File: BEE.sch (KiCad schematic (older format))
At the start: 53 parts, among them J1 RPI1_header, J10 Conn_01x02, J11 Conn_01x02, J12 Conn_01x02, J13 Conn_01x06, J14 Conn_01x03, J16 Conn_01x08, J17 Conn_01x03, J18 Conn_01x03, J2 Conn_02x05_Odd_Even, J3 Conn_02x03_Odd_Even, J4 Conn_01x06, J5 Conn_02x10_Odd_Even, J7 Conn_02x08_Odd_Even, J8 Conn_02x08_Top_Bottom, J9 Conn_01x02, SW1 SW_Push, SW2 SW_Push, SW3 SW_Push, U1 MCP3008, U2 MCP4911

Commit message: first version with display and dip switches
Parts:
- removed J3: Conn_02x03_Odd_Even, Connector_PinHeader_2.54mm:PinHeader_2x03_P2.54mm_Vertical, symbol Connector_Generic:Conn_02x03_Odd_Even
- removed J8: Conn_02x08_Top_Bottom, Connector_PinHeader_2.54mm:PinHeader_2x08_P2.54mm_Vertical, symbol Connector_Generic:Conn_02x08_Odd_Even
- removed U1: MCP3008, Package_SO:SOIC-16_3.9x9.9mm_P1.27mm, symbol Analog_ADC:MCP3008
- added C4: 0.1uF, Capacitor_SMD:C_0805_2012Metric_Pad1.18x1.45mm_HandSolder, symbol Device:C
- added J3: Conn_01x03, Connector_PinHeader_2.54mm:PinHeader_1x03_P2.54mm_Vertical, symbol Connector_Generic:Conn_01x03
- added J6: Conn_01x06, Connector_PinHeader_2.54mm:PinHeader_1x06_P2.54mm_Vertical, symbol Connector_Generic:Conn_01x06
- added R16, R17, R18, R19, R20, R21, R22, R23: 220, Resistor_SMD:R_0805_2012Metric_Pad1.20x1.40mm_HandSolder, symbol Device:R
- added U1: MCP3008, Package_SO:SOIC-16_3.9x9.9mm_P1.27mm, symbol BEE:MCP3008
- added U3, U4: Dip_08xsp3t, BEElib:dip_08xsp3t, symbol BEE:Dip_08xsp3t
- added U5: 74HC595, Package_SO:SOIC-16_3.9x9.9mm_P1.27mm, symbol 74xx:74HC595
- added U6: Display_7Segments, BEElib:7segments, symbol BEE:Display_7Segments
- C1, C2, C3: footprint Capacitor_SMD:C_0805_2012Metric_Pad1.15x1.40mm_HandSolder -> Capacitor_SMD:C_0805_2012Metric_Pad1.18x1.45mm_HandSolder
- R1, R15, R2, R3, R4, R5, R6, R7, R8: footprint Resistor_SMD:R_0805_2012Metric_Pad1.15x1.40mm_HandSolder -> Resistor_SMD:R_0805_2012Metric_Pad1.20x1.40mm_HandSolder
- R10: renamed from R9; footprint Resistor_SMD:R_0805_2012Metric_Pad1.15x1.40mm_HandSolder -> Resistor_SMD:R_0805_2012Metric_Pad1.20x1.40mm_HandSolder
- R11: renamed from R13; footprint Resistor_SMD:R_0805_2012Metric_Pad1.15x1.40mm_HandSolder -> Resistor_SMD:R_0805_2012Metric_Pad1.20x1.40mm_HandSolder
- R12: renamed from R14; footprint Resistor_SMD:R_0805_2012Metric_Pad1.15x1.40mm_HandSolder -> Resistor_SMD:R_0805_2012Metric_Pad1.20x1.40mm_HandSolder
- R13: renamed from R10; footprint Resistor_SMD:R_0805_2012Metric_Pad1.15x1.40mm_HandSolder -> Resistor_SMD:R_0805_2012Metric_Pad1.20x1.40mm_HandSolder
- R14: renamed from R11; footprint Resistor_SMD:R_0805_2012Metric_Pad1.15x1.40mm_HandSolder -> Resistor_SMD:R_0805_2012Metric_Pad1.20x1.40mm_HandSolder
- R9: renamed from R12; footprint Resistor_SMD:R_0805_2012Metric_Pad1.15x1.40mm_HandSolder -> Resistor_SMD:R_0805_2012Metric_Pad1.20x1.40mm_HandSolder
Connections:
- net labels added: BCM18, QH', RCLK, SER, SRCLK, nOE, nSRCLR
- net labels removed: AR0, AR1, AR2, AR3, AR4, AR5, AR6, AR7, BCM18_PWM0
- wire segments 246 -> 275
- no-connect marks 6 -> 5
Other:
- note added: "7/8 Segment Display Driver"
- note added: "QH'"
- note added: "RCLK"
- note added: "SER"
- note added: "SRCLK"
- note added: "Socket (feemale)"
- note added: "UART: FTDI cables:\n1 - Black -> gnd\n2 - Brown -> CTS\n3 - Red -> Vcc\n4 - Orange -> TX\n5 - Yellow -> RX\n6 - Green -> RTS\n\nWe connect them crossed"
- note added: "nOE"
- note added: "nSRCLR\n"
- note removed: "Resistor set to polarrize external analog sensors"
- note removed: "UART. TDI cables:\n1 - Black -> gnd\n2 - Brown -> CTS\n3 - Red -> Vcc\n4 - Orange -> TX\n5 - Yellow -> RX\n6 - Green -> RTS\n\nWe connect them crossed"
- moved on the sheet: BZ1, C1, C2, C3, FID1, FID2, FID3, H1, H2, H3, H4, J10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

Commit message: Bypass cap for Shifter, DAC cap symbol fix, DAC out pin headers reorganization, labels and fab layer cleanup.
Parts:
- added C5: 0.1uF, Capacitor_SMD:C_0805_2012Metric_Pad1.18x1.45mm_HandSolder, symbol Device:C
- C3: footprint Capacitor_SMD:C_0805_2012Metric_Pad1.18x1.45mm_HandSolder -> Capacitor_Tantalum_SMD:CP_EIA-2012-15_AVX-P_Pad1.30x1.05mm_HandSolder; symbol Device:C -> Device:CP1
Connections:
- net GND: now also C5.1
- net at J10.1 (Pin_1), U2.6 (Vref): now also C5.2
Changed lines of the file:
@@
 	9455 3405 9505 3405
 Wire Wire Line
-	8955 3305 9355 3305
+	8955 3305 9025 3305
 $Comp
 L power:PWR_FLAG #FLG0102
@@
 Wire Wire Line
 	8055 3605 8355 3605
-$Comp
-L Device:C C2
-U 1 1 5D974B40
-P 8355 3055
-F 0 "C2" V 8305 3155 50  0000 C CNN
-F 1 "0.1uF" V 8255 2905 50  0000 C CNN
-F 2 "Capacitor_SMD:C_0805_2012Metric_Pad1.18x1.45mm_HandSolder" H 8393 2905 50  0001 C CNN
-F 3 "https://www.mouser.es/datasheet/2/212/KEM_C1002_X7R_SMD-1102033.pdf" H 8355 3055 50  0001 C CNN
-F 4 "Mouser" H 5   -195 50  0001 C CNN "Distributor"
-F 5 "80-C0805C104K3R" H 5   -195 50  0001 C CNN "Distributor PN"
-F 6 "https://www.mouser.es/ProductDetail/KEMET/C0805C104K3RACTU?qs=sGAEpiMZZMs0AnBnWHyRQFCCI5cSbRT%2FqS%252BgegeU2mQ%3D" H 5   -195 50  0001 C CNN "Distributor link"
-F 7 "KEMET" H 5   -195 50  0001 C CNN "Manufacturer"
-F 8 "C0805C104K3RACTU" H 5   -195 50  0001 C CNN "Manufacturer PN"
-	1    8355 3055
-	0    1    1    0
-$EndComp
-$Comp
-L Device:C C3
-U 1 1 5D974BE9
-P 8355 3255
-F 0 "C3" V 8305 3355 50  0000 C CNN
-F 1 "10uF" V 8305 3105 50  0000 C CNN
-F 2 "Capacitor_SMD:C_0805_2012Metric_Pad1.18x1.45mm_HandSolder" H 8393 3105 50  0001 C CNN
-F 3 "https://www.mouser.es/datasheet/2/40/TAJ_LOW_PROFILE-932651.pdf" H 8355 3255 50  0001 C CNN
-F 4 "Mouser" H 5   -195 50  0001 C CNN "Distributor"
-F 5 " 581-TAJP106K006RNJ " H 5   -195 50  0001 C CNN "Distributor PN"
-F 6 "https://www.mouser.es/ProductDetail/AVX/TAJP106K006RNJ?qs=q%252BHV0zBR8MhWDNAZ3JBdYA%3D%3D" H 5   -195 50  0001 C CNN "Distributor link"
-F 7 "AVX" H 5   -195 50  0001 C CNN "Manufacturer"
-F 8 "TAJP106K006RNJ " H 5   -195 50  0001 C CNN "Manufacturer PN"
-	1    8355 3255
-	0    1    1    0
-$EndComp
 Connection ~ 8755 3255
 Wire Wire Line
@@
 Text Label 7915 1945 0    50   ~ 0
 QH'
+$Comp
+L Device:C C5
+U 1 1 62DC27FC
+P 9025 3155
+F 0 "C5" V 8975 3255 50  0000 C CNN
+F 1 "0.1uF" V 8890 3155 50  0000 C CNN
+F 2 "Capacitor_SMD:C_0805_2012Metric_Pad1.18x1.45mm_HandSolder" H 9063 3005 50  0001 C CNN
+F 3 "https://www.mouser.es/datasheet/2/212/KEM_C1002_X7R_SMD-1102033.pdf" H 9025 3155 50  0001 C CNN
+F 4 "Mouser" H 675 -95 50  0001 C CNN "Distributor"
+F 5 "80-C0805C104K3R" H 675 -95 50  0001 C CNN "Distributor PN"
+F 6 "https://www.mouser.es/ProductDetail/KEMET/C0805C104K3RACTU?qs=sGAEpiMZZMs0AnBnWHyRQFCCI5cSbRT%2FqS%252BgegeU2mQ%3D" H 675 -95 50  0001 C CNN "Distributor link"
+F 7 "KEMET" H 675 -95 50  0001 C CNN "Manufacturer"
+F 8 "C0805C104K3RACTU" H 675 -95 50  0001 C CNN "Manufacturer PN"
+	1    9025 3155
+	1    0    0    -1
+$EndComp
+Connection ~ 9025 3305
+Wire Wire Line
+	9025 3305 9355 3305
+$Comp
+L power:GND #PWR038
+U 1 1 62DC48E1
+P 9215 2955
+F 0 "#PWR038" H 9215 2705 50  0001 C CNN
+F 1 "GND" H 9315 2955 50  0000 C CNN
+F 2 "" H 9215 2955 50  0001 C CNN
+F 3 "" H 9215 2955 50  0001 C CNN
+	1    9215 2955
+	1    0    0    -1
+$EndComp
+Wire Wire Line
+	9215 2955 9215 2945
+Wire Wire Line
+	9215 2945 9025 2945
+Wire Wire Line
+	9025 2945 9025 3005
+$Comp
+L Device:CP1 C3
+U 1 1 5D974BE9
+P 8355 3255
+F 0 "C3" V 8485 3255 50  0000 C CNN
+F 1 "10uF" V 8305 3105 50  0000 C CNN
+F 2 "Capacitor_Tantalum_SMD:CP_EIA-2012-15_AVX-P_Pad1.30x1.05mm_HandSolder" H 8393 3105 50  0001 C CNN
+F 3 "https://www.mouser.es/datasheet/2/40/TAJ_LOW_PROFILE-932651.pdf" H 8355 3255 50  0001 C CNN
+F 4 "Mouser" H 5   -195 50  0001 C CNN "Distributor"
+F 5 " 581-TAJP106K006RNJ " H 5   -195 50  0001 C CNN "Distributor PN"
+F 6 "https://www.mouser.es/ProductDetail/AVX/TAJP106K006RNJ?qs=q%252BHV0zBR8MhWDNAZ3JBdYA%3D%3D" H 5   -195 50  0001 C CNN "Distributor link"
+F 7 "AVX" H 5   -195 50  0001 C CNN "Manufacturer"
+F 8 "TAJP106K006RNJ " H 5   -195 50  0001 C CNN "Manufacturer PN"
+	1    8355 3255
+	0    1    1    0
+$EndComp
+$Comp
+L Device:C C2
+U 1 1 5D974B40
+P 8355 3055
+F 0 "C2" V 8230 3055 50  0000 C CNN
+F 1 "0.1uF" V 8305 2900 50  0000 C CNN
+F 2 "Capacitor_SMD:C_0805_2012Metric_Pad1.18x1.45mm_HandSolder" H 8393 2905 50  0001 C CNN
+F 3 "https://www.mouser.es/datasheet/2/212/KEM_C1002_X7R_SMD-1102033.pdf" H 8355 3055 50  0001 C CNN
+F 4 "Mouser" H 5   -195 50  0001 C CNN "Distributor"
+F 5 "80-C0805C104K3R" H 5   -195 50  0001 C CNN "Distributor PN"
+F 6 "https://www.mouser.es/ProductDetail/KEMET/C0805C104K3RACTU?qs=sGAEpiMZZMs0AnBnWHyRQFCCI5cSbRT%2FqS%252BgegeU2mQ%3D" H 5   -195 50  0001 C CNN "Distributor link"
+F 7 "KEMET" H 5   -195 50  0001 C CNN "Manufacturer"
+F 8 "C0805C104K3RACTU" H 5   -195 50  0001 C CNN "Manufacturer PN"
+	1    8355 3055
+	0    1    1    0
+$EndComp
 $EndSCHEMATC

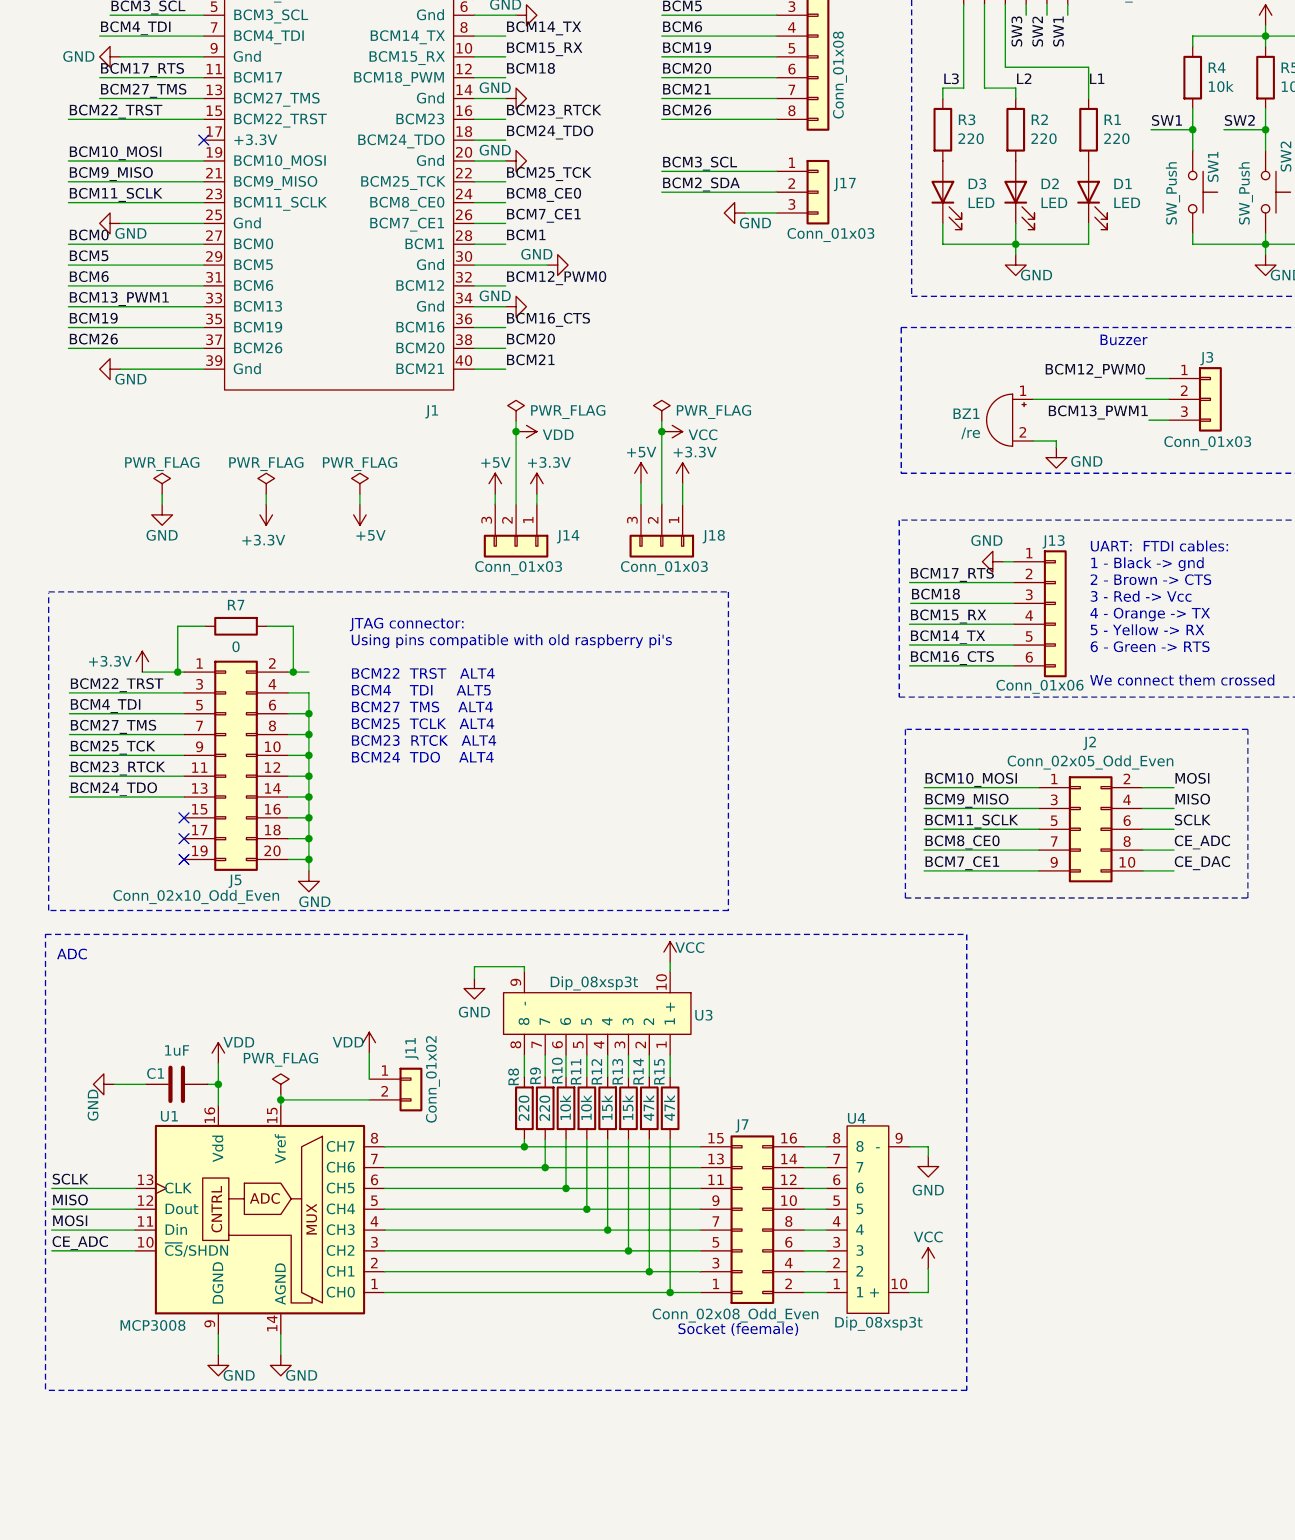
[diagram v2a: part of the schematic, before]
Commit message: independent polarization network
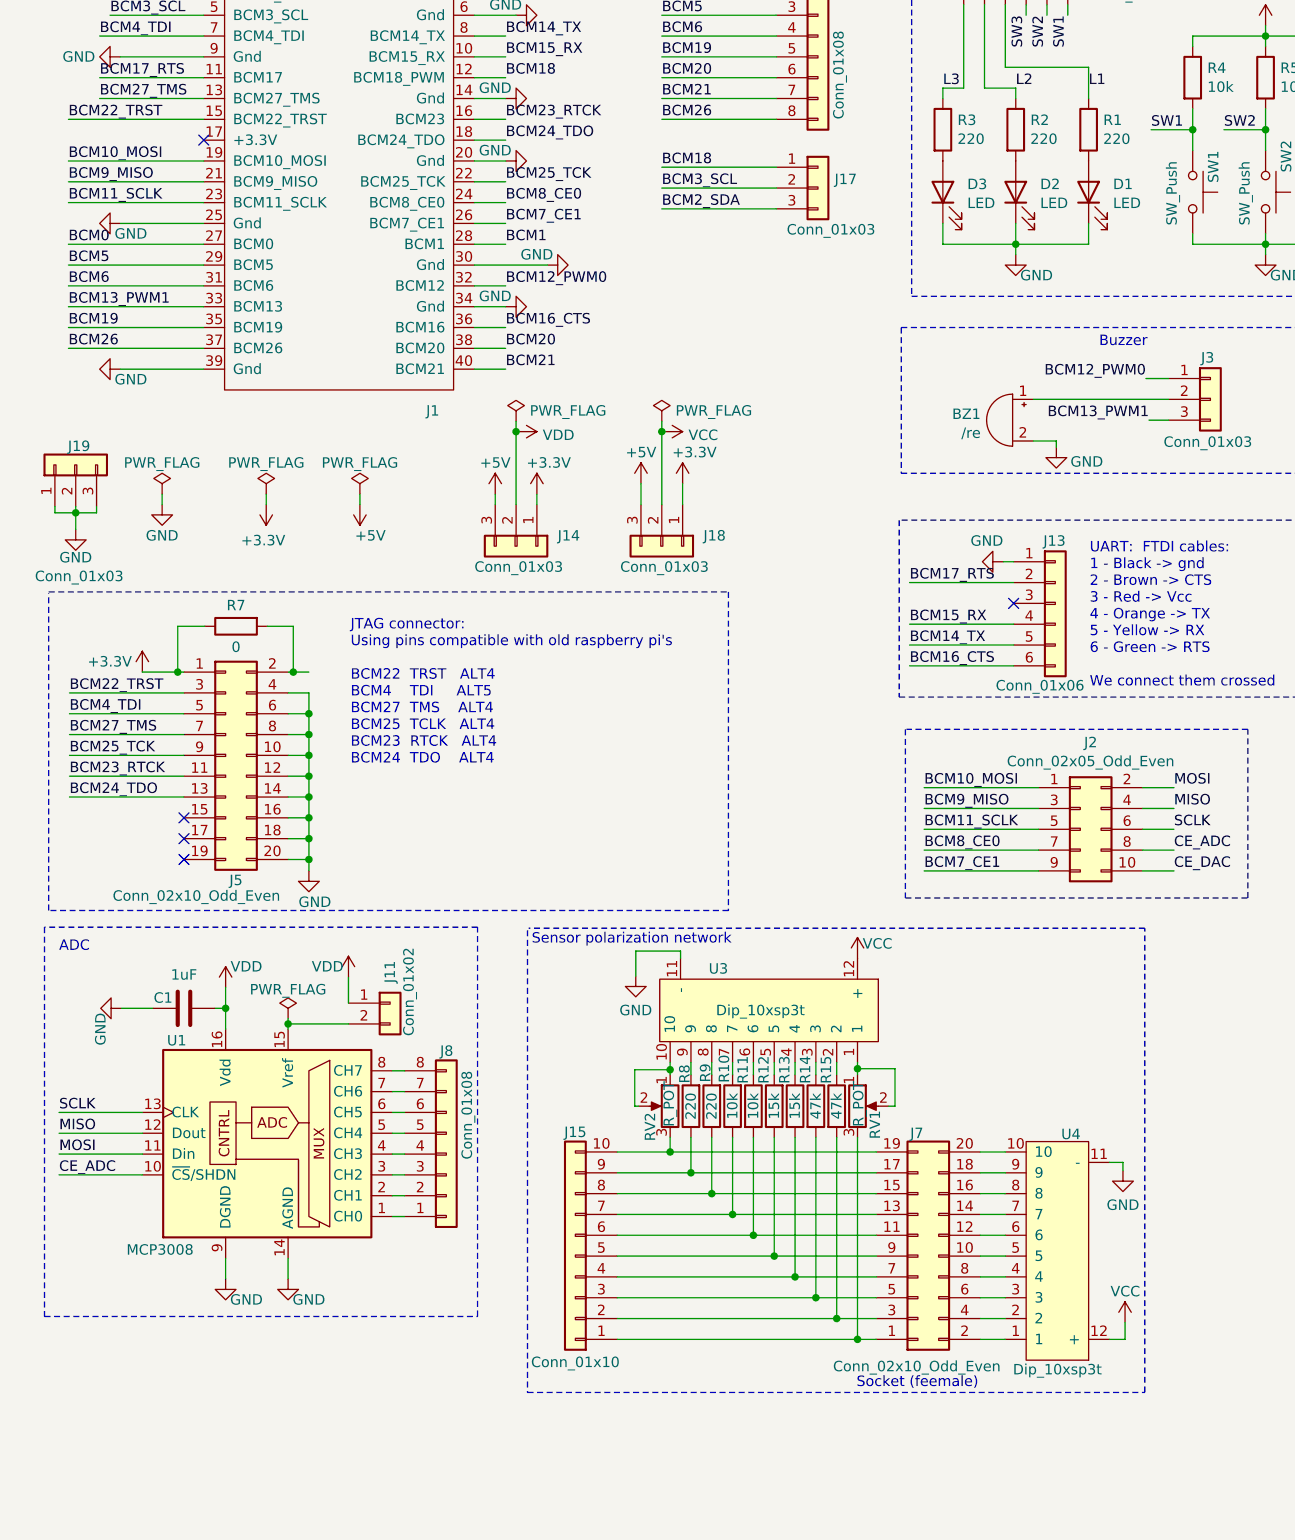
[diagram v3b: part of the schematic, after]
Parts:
- removed J7: Conn_02x08_Odd_Even, Connector_PinSocket_2.54mm:PinSocket_2x08_P2.54mm_Vertical, symbol Connector_Generic:Conn_02x08_Odd_Even
- removed U3, U4: Dip_08xsp3t, BEElib:dip_08xsp3t, symbol BEE:Dip_08xsp3t
- added J15: Conn_01x10, Connector_PinHeader_2.54mm:PinHeader_1x10_P2.54mm_Vertical, symbol Connector_Generic:Conn_01x10
- added J19: Conn_01x03, Connector_PinHeader_2.54mm:PinHeader_1x03_P2.54mm_Vertical, symbol Connector_Generic:Conn_01x03
- added J7: Conn_02x10_Odd_Even, Connector_PinSocket_2.54mm:PinSocket_2x10_P2.54mm_Vertical, symbol Connector_Generic:Conn_02x10_Odd_Even
- added J8: Conn_01x08, Connector_PinHeader_2.54mm:PinHeader_1x08_P2.54mm_Vertical, symbol Connector_Generic:Conn_01x08
- added RV1, RV2: R_POT, BEElib:POT_PVG5A, symbol Device:R_POT
- added U3, U4: Dip_10xsp3t, BEElib:dip_10xsp3t, symbol BEE:Dip_10xsp3t
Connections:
- net BCM18: now also J17.1 (Pin_1); no longer J13.3 (Pin_3)
- net BCM2_SDA: now also J17.3 (Pin_3); no longer J17.2 (Pin_2)
- net BCM3_SCL: now also J17.2 (Pin_2); no longer J17.1 (Pin_1)
- net GND: now also J19.1 (Pin_1), J19.2 (Pin_2), J19.3 (Pin_3), U3.11 (-), U4.11 (-); no longer J17.3 (Pin_3)
- net VCC: now also U3.12 (+), U4.12 (+)
- net at R9.1: now also J15.8 (Pin_8), J7.15 (Pin_15); no longer U1.7 (CH6)
- net at R9.2: now also U3.8
- net at R15.2: now also J15.2 (Pin_2), J7.3 (Pin_3); no longer U1.1 (CH0)
- net at R10.1: now also J15.7 (Pin_7), J7.13 (Pin_13); no longer U1.6 (CH5)
- net at R8.1: now also J15.9 (Pin_9), J7.17 (Pin_17); no longer U1.8 (CH7)
- net at R14.2: now also J15.3 (Pin_3), J7.5 (Pin_5); no longer U1.2 (CH1)
- net at R13.2: now also J15.4 (Pin_4), J7.7 (Pin_7); no longer U1.3 (CH2)
- net at R12.1: now also J15.5 (Pin_5), J7.9 (Pin_9); no longer U1.4 (CH3)
- net at R11.2: now also J15.6 (Pin_6), J7.11 (Pin_11); no longer U1.5 (CH4)
- net at R11.1: now also U3.6
- net at R12.2: now also U3.5
- net at R15.1: now also U3.2
- net at R14.1: now also U3.3
- net at R13.1: now also U3.4
- net at R10.2: now also U3.7
- net at R8.2: now also U3.9
- new net: J8.1 (Pin_1), U1.1 (CH0)
- new net: J8.2 (Pin_2), U1.2 (CH1)
- new net: J8.3 (Pin_3), U1.3 (CH2)
- new net: J8.4 (Pin_4), U1.4 (CH3)
- new net: J8.5 (Pin_5), U1.5 (CH4)
- new net: J8.6 (Pin_6), U1.6 (CH5)
- new net: J8.7 (Pin_7), U1.7 (CH6)
- new net: J8.8 (Pin_8), U1.8 (CH7)
- new net: RV1.1, RV1.2, U3.1
- new net: J15.1 (Pin_1), J7.1 (Pin_1), RV1.3
- new net: RV2.1, RV2.2, U3.10
- new net: J7.2 (Pin_2), U4.1
- new net: J7.20 (Pin_20), U4.10
- new net: J7.4 (Pin_4), U4.2
- new net: J7.6 (Pin_6), U4.3
- new net: J7.8 (Pin_8), U4.4
- new net: J7.10 (Pin_10), U4.5
- new net: J7.12 (Pin_12), U4.6
- new net: J7.14 (Pin_14), U4.7
- new net: J7.16 (Pin_16), U4.8
- new net: J7.18 (Pin_18), U4.9
- new net: J15.10 (Pin_10), J7.19 (Pin_19), RV2.3
- no-connect marks 5 -> 6
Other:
- note added: "Sensor polarization network"
- moved on the sheet: C1, J11, J17, R10, R11, R12, R13, R14, R15, R8, R9, U1
